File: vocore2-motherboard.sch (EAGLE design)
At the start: 100 parts, among them IC1 AP63205, IC2 FE1.1S, IC3 LM3671MF-3.3, IC4 LM3671MF-3.3, IC5 LM3671MF-3.3, IC7 SN74LVC2G14DBVR, IC8 FT230XS-R, J1 RJHSE-5381, J2 TE_1775470-8, J3 AMPHENOL_1140084168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

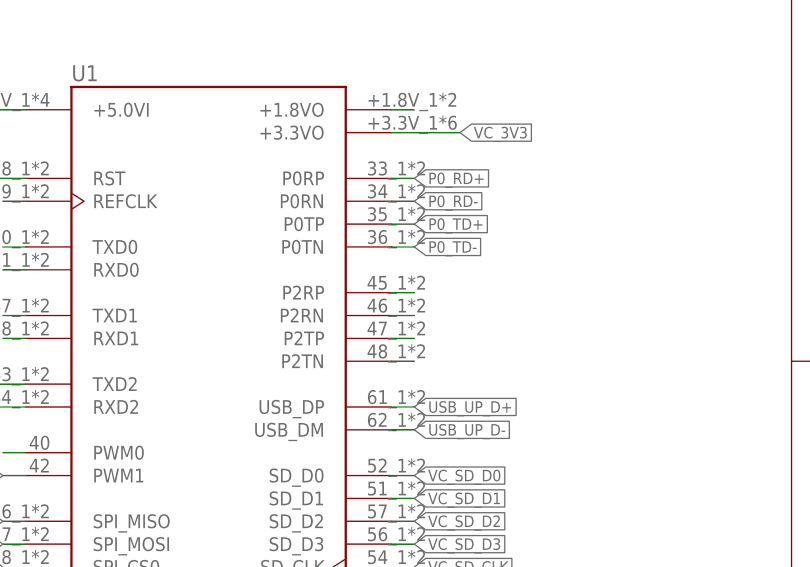
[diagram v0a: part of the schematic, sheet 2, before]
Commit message: fix(pcb): reconnected buzzer
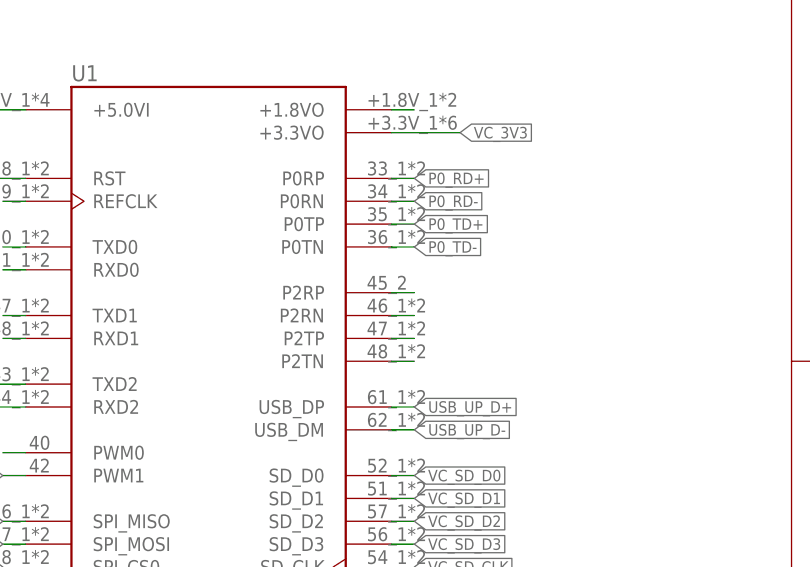
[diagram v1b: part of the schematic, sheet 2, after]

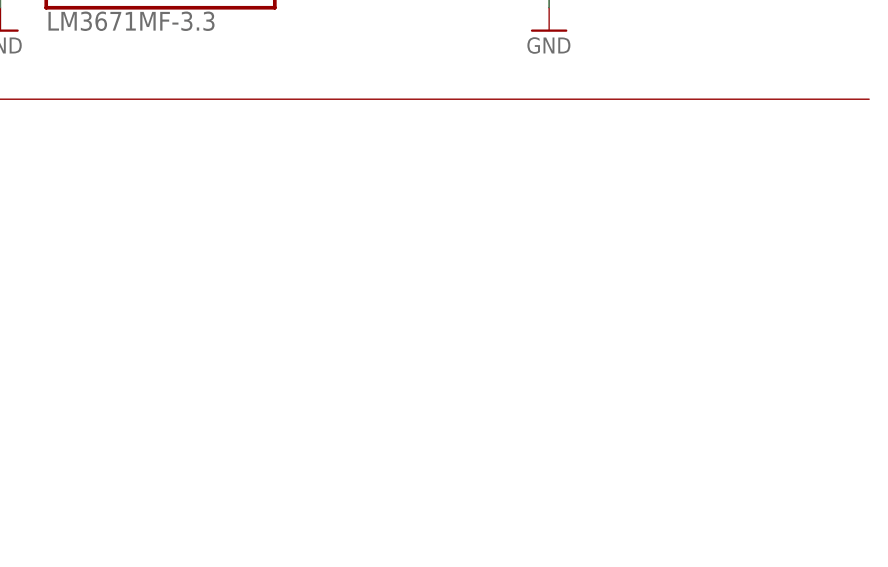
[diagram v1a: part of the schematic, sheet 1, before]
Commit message: feat: 3V3 + GND pinheader for each minipcie-slot
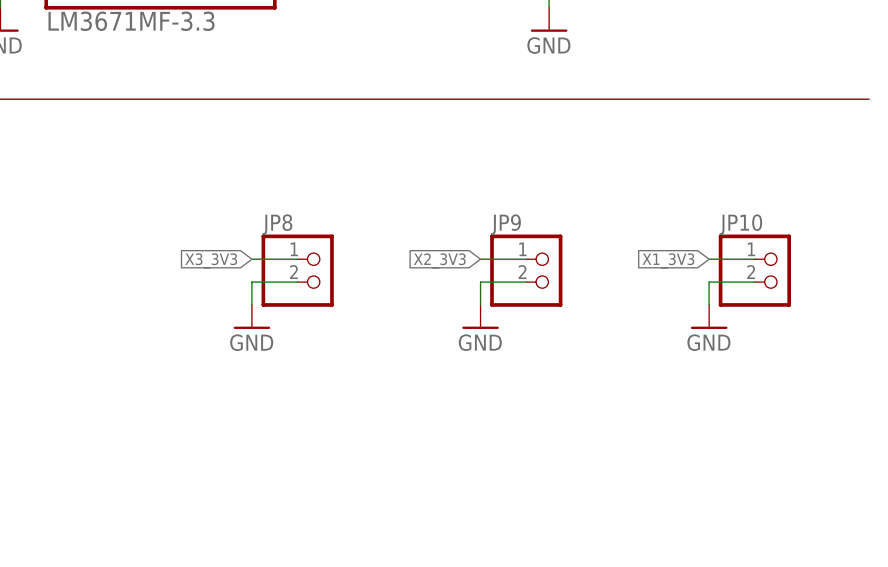
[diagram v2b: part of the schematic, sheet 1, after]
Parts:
- added JP10, JP8, JP9: (no value), pinhead:PINHD-1X2
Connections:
- net GND: now also JP10.2, JP8.2, JP9.2
- net X1_3V3: now also JP10.1
- net X2_3V3: now also JP9.1
- net X3_3V3: now also JP8.1
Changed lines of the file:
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@@
 <part name="GND29" library="supply1" deviceset="GND" device=""/>
 <part name="R22" library="rcl" library_urn="urn:adsk.eagle:library:334" deviceset="R-EU_" device="R0603" package3d_urn="urn:adsk.eagle:package:23555/3" value="330R"/>
+<part name="JP8" library="pinhead" library_urn="urn:adsk.eagle:library:325" deviceset="PINHD-1X2" device="" package3d_urn="urn:adsk.eagle:package:22435/2"/>
+<part name="GND30" library="supply1" deviceset="GND" device=""/>
+<part name="JP9" library="pinhead" library_urn="urn:adsk.eagle:library:325" deviceset="PINHD-1X2" device="" package3d_urn="urn:adsk.eagle:package:22435/2"/>
+<part name="JP10" library="pinhead" library_urn="urn:adsk.eagle:library:325" deviceset="PINHD-1X2" device="" package3d_urn="urn:adsk.eagle:package:22435/2"/>
+<part name="GND45" library="supply1" deviceset="GND" device=""/>
+<part name="GND46" library="supply1" deviceset="GND" device=""/>
 </parts>
 <sheets>
@@
 <attribute name="VALUE" x="132.08" y="33.02" size="1.778" layer="96"/>
 </instance>
+<instance part="JP8" gate="G$1" x="195.58" y="48.26" smashed="yes">
+<attribute name="NAME" x="189.23" y="53.975" size="1.778" layer="95"/>
+<attribute name="VALUE" x="189.23" y="43.18" size="1.778" layer="96"/>
+</instance>
+<instance part="GND30" gate="1" x="187.96" y="43.18" smashed="yes">
+<attribute name="VALUE" x="185.42" y="40.64" size="1.778" layer="96"/>
+</instance>
+<instance part="JP9" gate="G$1" x="220.98" y="48.26" smashed="yes">
+<attribute name="NAME" x="214.63" y="53.975" size="1.778" layer="95"/>
+<attribute name="VALUE" x="214.63" y="43.18" size="1.778" layer="96"/>
+</instance>
+<instance part="JP10" gate="G$1" x="246.38" y="48.26" smashed="yes">
+<attribute name="NAME" x="240.03" y="53.975" size="1.778" layer="95"/>
+<attribute name="VALUE" x="240.03" y="43.18" size="1.778" layer="96"/>
+</instance>
+<instance part="GND45" gate="1" x="213.36" y="43.18" smashed="yes">
+<attribute name="VALUE" x="210.82" y="40.64" size="1.778" layer="96"/>
+</instance>
+<instance part="GND46" gate="1" x="238.76" y="43.18" smashed="yes">
+<attribute name="VALUE" x="236.22" y="40.64" size="1.778" layer="96"/>
+</instance>
 </instances>
 <busses>
@@
 <wire x1="134.62" y1="40.64" x2="134.62" y2="38.1" width="0.1524" layer="91"/>
 <pinref part="GND36" gate="1" pin="GND"/>
+</segment>
+<segment>
+<pinref part="JP8" gate="G$1" pin="2"/>
+<wire x1="193.04" y1="48.26" x2="187.96" y2="48.26" width="0.1524" layer="91"/>
+<wire x1="187.96" y1="48.26" x2="187.96" y2="45.72" width="0.1524" layer="91"/>
+<pinref part="GND30" gate="1" pin="GND"/>
+</segment>
+<segment>
+<pinref part="JP9" gate="G$1" pin="2"/>
+<wire x1="218.44" y1="48.26" x2="213.36" y2="48.26" width="0.1524" layer="91"/>
+<wire x1="213.36" y1="48.26" x2="213.36" y2="45.72" width="0.1524" layer="91"/>
+<pinref part="GND45" gate="1" pin="GND"/>
+</segment>
+<segment>
+<pinref part="JP10" gate="G$1" pin="2"/>
+<wire x1="243.84" y1="48.26" x2="238.76" y2="48.26" width="0.1524" layer="91"/>
+<wire x1="238.76" y1="48.26" x2="238.76" y2="45.72" width="0.1524" layer="91"/>
+<pinref part="GND46" gate="1" pin="GND"/>
 </segment>
 </net>
@@
 <pinref part="R2" gate="G$1" pin="2"/>
 </segment>
+<segment>
+<pinref part="JP10" gate="G$1" pin="1"/>
+<wire x1="243.84" y1="50.8" x2="238.76" y2="50.8" width="0.1524" layer="91"/>
+<label x="238.76" y="50.8" size="1.27" layer="95" rot="R180" xref="yes"/>
+</segment>
 </net>
 <net name="N$6" class="0">
@@
 <pinref part="R4" gate="G$1" pin="2"/>
 </segment>
+<segment>
+<pinref part="JP9" gate="G$1" pin="1"/>
+<wire x1="218.44" y1="50.8" x2="213.36" y2="50.8" width="0.1524" layer="91"/>
+<label x="213.36" y="50.8" size="1.27" layer="95" rot="R180" xref="yes"/>
+</segment>
 </net>
 <net name="X3_3V3" class="0">
@@
 <pinref part="R5" gate="G$1" pin="2"/>
 </segment>
-</net>
+<segment>
+<pinref part="JP8" gate="G$1" pin="1"/>
+<wire x1="193.04" y1="50.8" x2="187.96" y2="50.8" width="0.1524" layer="91"/>
+<label x="187.96" y="50.8" size="1.27" layer="95" rot="R180" xref="yes"/>
+</segment>
+</net>

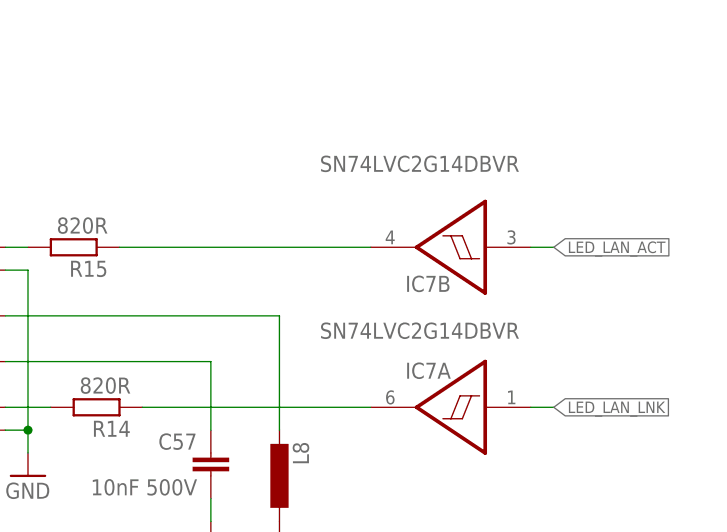
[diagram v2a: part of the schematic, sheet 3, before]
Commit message: fix: use non-inverting buffers to drive lan leds
The rt3050 ethernet switch, integrated on the SoC, has the ability to
configure led polarity. Therefore it is not necessary to fix the
active-low problem in hardware.
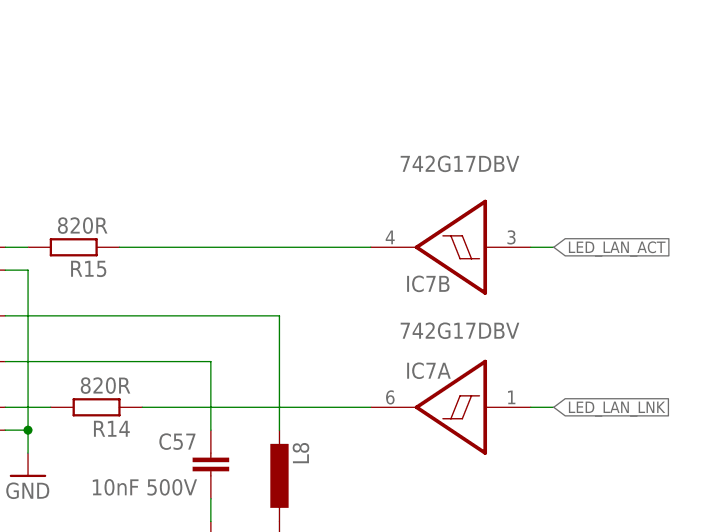
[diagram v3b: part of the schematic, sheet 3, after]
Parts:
- IC7: value SN74LVC2G14DBVR -> 742G17DBV
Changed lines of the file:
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@@
 <attribute name="DIGIKEY" value="A129687CT-ND"/>
 </part>
-<part name="IC7" library="74xx-little-de" library_urn="urn:adsk.eagle:library:86" deviceset="74*2G17" device="DBV" value="SN74LVC2G14DBVR">
+<part name="IC7" library="74xx-little-de" library_urn="urn:adsk.eagle:library:86" deviceset="74*2G17" device="DBV" value="742G17DBV">
 <attribute name="DIGIKEY" value="296-13010-1-ND"/>
 </part>

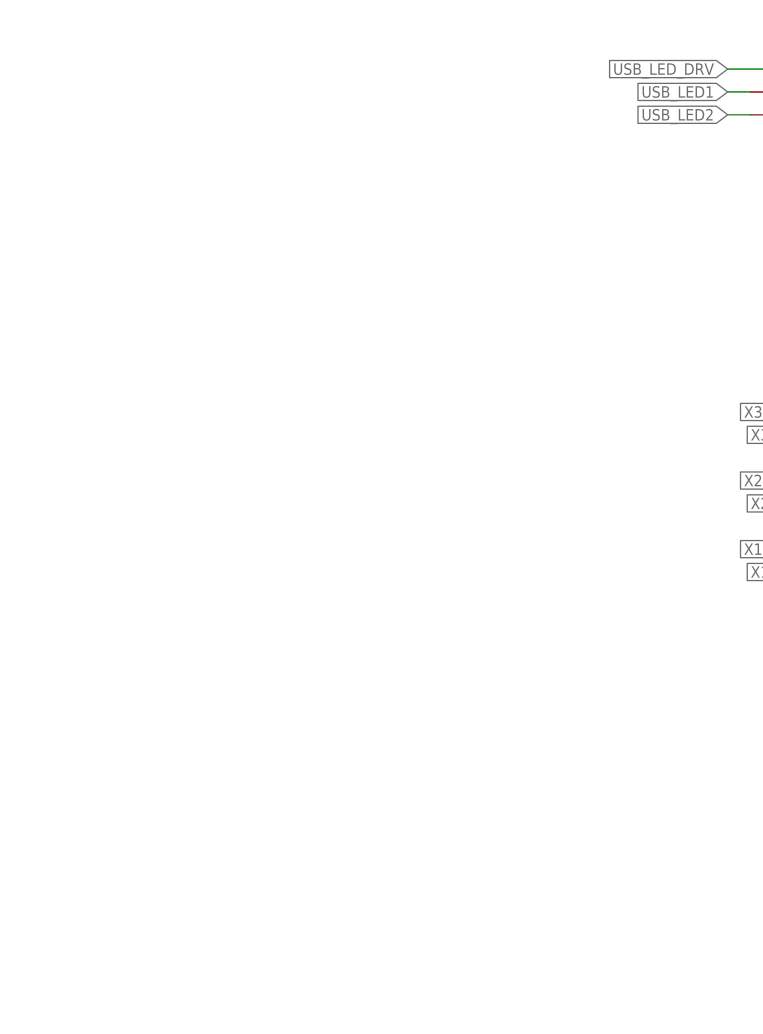
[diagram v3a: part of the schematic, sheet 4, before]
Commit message: feat: TVS diodes on MiniPCIe slots
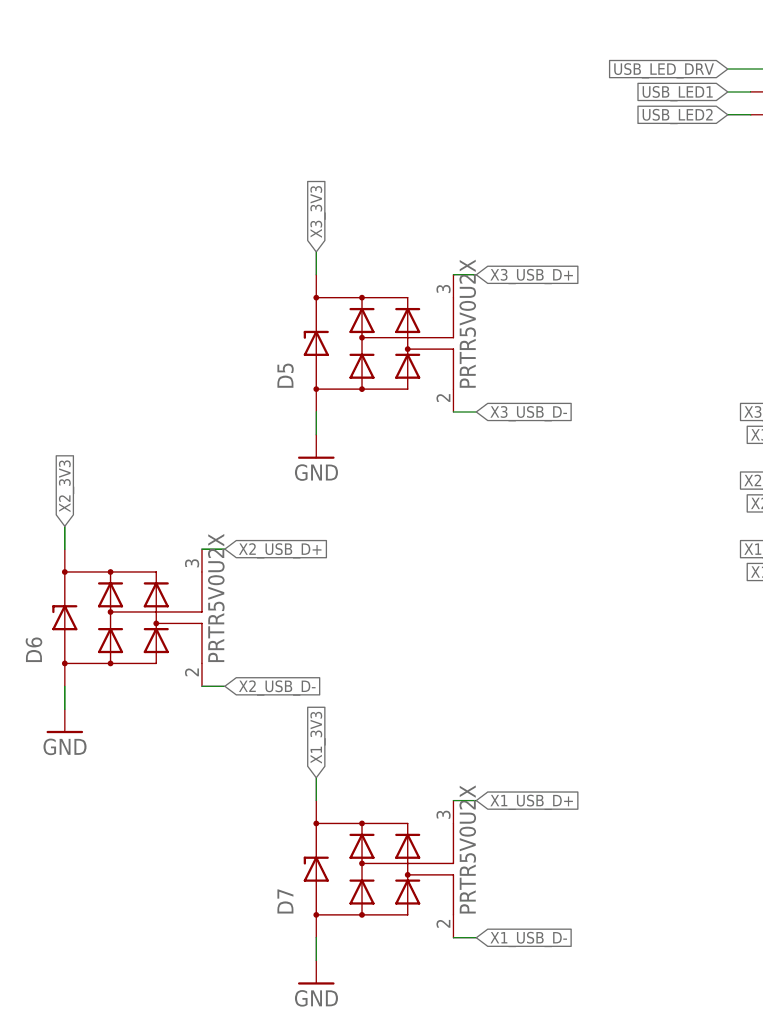
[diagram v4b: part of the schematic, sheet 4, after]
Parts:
- added D5, D6, D7: PRTR5V0U2X, diode:PRTR5V0U2X
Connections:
- net GND: now also D5.GND, D6.GND, D7.GND
- net X1_3V3: now also D7.VCC
- net X1_USB_D+: now also D7.IO2
- net X1_USB_D-: now also D7.IO1
- net X2_3V3: now also D6.VCC
- net X2_USB_D+: now also D6.IO2
- net X2_USB_D-: now also D6.IO1
- net X3_3V3: now also D5.VCC
- net X3_USB_D+: now also D5.IO2
- net X3_USB_D-: now also D5.IO1
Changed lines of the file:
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@@
 <part name="GND45" library="supply1" deviceset="GND" device=""/>
 <part name="GND46" library="supply1" deviceset="GND" device=""/>
+<part name="D5" library="diode" library_urn="urn:adsk.eagle:library:210" deviceset="PRTR5V0U2X" device="">
+<attribute name="DIGIKEY" value="1727-3884-1-ND"/>
+<attribute name="FARNELL" value="1524157"/>
+</part>
+<part name="D6" library="diode" library_urn="urn:adsk.eagle:library:210" deviceset="PRTR5V0U2X" device="">
+<attribute name="DIGIKEY" value="1727-3884-1-ND"/>
+<attribute name="FARNELL" value="1524157"/>
+</part>
+<part name="D7" library="diode" library_urn="urn:adsk.eagle:library:210" deviceset="PRTR5V0U2X" device="">
+<attribute name="DIGIKEY" value="1727-3884-1-ND"/>
+<attribute name="FARNELL" value="1524157"/>
+</part>
+<part name="GND47" library="supply1" library_urn="urn:adsk.eagle:library:371" deviceset="GND" device="">
+<attribute name="SPICEPREFIX" value="G"/>
+</part>
+<part name="GND48" library="supply1" library_urn="urn:adsk.eagle:library:371" deviceset="GND" device="">
+<attribute name="SPICEPREFIX" value="G"/>
+</part>
+<part name="GND49" library="supply1" library_urn="urn:adsk.eagle:library:371" deviceset="GND" device="">
+<attribute name="SPICEPREFIX" value="G"/>
+</part>
 </parts>
 <sheets>
@@
 <attribute name="VALUE" x="153.035" y="53.848" size="1.778" layer="96" rot="R90"/>
 <attribute name="DIGIKEY" x="147.32" y="58.42" size="1.778" layer="96" display="off"/>
+</instance>
+<instance part="D5" gate="G$1" x="-22.86" y="38.1" smashed="yes" rot="R90">
+<attribute name="FARNELL" x="-22.86" y="38.1" size="1.778" layer="96" rot="R90" display="off"/>
+<attribute name="NAME" x="-33.02" y="32.9565" size="1.778" layer="95" rot="R90"/>
+<attribute name="VALUE" x="-12.7635" y="32.9565" size="1.778" layer="96" rot="R90"/>
+<attribute name="DIGIKEY" x="-22.86" y="38.1" size="1.778" layer="96" rot="R90" display="off"/>
+</instance>
+<instance part="D6" gate="G$1" x="-50.8" y="7.62" smashed="yes" rot="R90">
+<attribute name="FARNELL" x="-50.8" y="7.62" size="1.778" layer="96" rot="R90" display="off"/>
+<attribute name="NAME" x="-60.96" y="2.4765" size="1.778" layer="95" rot="R90"/>
+<attribute name="VALUE" x="-40.7035" y="2.4765" size="1.778" layer="96" rot="R90"/>
+<attribute name="DIGIKEY" x="-50.8" y="7.62" size="1.778" layer="96" rot="R90" display="off"/>
+</instance>
+<instance part="D7" gate="G$1" x="-22.86" y="-20.32" smashed="yes" rot="R90">
+<attribute name="FARNELL" x="-22.86" y="-20.32" size="1.778" layer="96" rot="R90" display="off"/>
+<attribute name="NAME" x="-33.02" y="-25.4635" size="1.778" layer="95" rot="R90"/>
+<attribute name="VALUE" x="-12.7635" y="-25.4635" size="1.778" layer="96" rot="R90"/>
+<attribute name="DIGIKEY" x="-22.86" y="-20.32" size="1.778" layer="96" rot="R90" display="off"/>
+</instance>
+<instance part="GND47" gate="1" x="-30.48" y="25.4" smashed="yes" rot="MR0">
+<attribute name="VALUE" x="-27.94" y="22.86" size="1.778" layer="96" rot="MR0"/>
+</instance>
+<instance part="GND48" gate="1" x="-58.42" y="-5.08" smashed="yes" rot="MR0">
+<attribute name="VALUE" x="-55.88" y="-7.62" size="1.778" layer="96" rot="MR0"/>
+</instance>
+<instance part="GND49" gate="1" x="-30.48" y="-33.02" smashed="yes" rot="MR0">
+<attribute name="VALUE" x="-27.94" y="-35.56" size="1.778" layer="96" rot="MR0"/>
 </instance>
 </instances>
@@
 <pinref part="GND23" gate="1" pin="GND"/>
 </segment>
+<segment>
+<pinref part="D5" gate="G$1" pin="GND"/>
+<wire x1="-30.48" y1="30.48" x2="-30.48" y2="27.94" width="0.1524" layer="91"/>
+<pinref part="GND47" gate="1" pin="GND"/>
+</segment>
+<segment>
+<pinref part="D6" gate="G$1" pin="GND"/>
+<wire x1="-58.42" y1="0" x2="-58.42" y2="-2.54" width="0.1524" layer="91"/>
+<pinref part="GND48" gate="1" pin="GND"/>
+</segment>
+<segment>
+<pinref part="D7" gate="G$1" pin="GND"/>
+<wire x1="-30.48" y1="-27.94" x2="-30.48" y2="-30.48" width="0.1524" layer="91"/>
+<pinref part="GND49" gate="1" pin="GND"/>
+</segment>
 </net>
 <net name="USB_UP_D-" class="0">
@@
 <label x="27.94" y="15.24" size="1.27" layer="95" rot="MR0" xref="yes"/>
 </segment>
+<segment>
+<pinref part="D7" gate="G$1" pin="IO2"/>
+<wire x1="-15.24" y1="-12.7" x2="-12.7" y2="-12.7" width="0.1524" layer="91"/>
+<label x="-12.7" y="-12.7" size="1.27" layer="95" xref="yes"/>
+</segment>
 </net>
 <net name="X1_USB_D-" class="0">
@@
 <label x="27.94" y="12.7" size="1.27" layer="95" rot="MR0" xref="yes"/>
 </segment>
+<segment>
+<pinref part="D7" gate="G$1" pin="IO1"/>
+<wire x1="-15.24" y1="-27.94" x2="-12.7" y2="-27.94" width="0.1524" layer="91"/>
+<label x="-12.7" y="-27.94" size="1.27" layer="95" xref="yes"/>
+</segment>
 </net>
 <net name="X3_USB_D+" class="0">
@@
 <wire x1="30.48" y1="30.48" x2="27.94" y2="30.48" width="0.1524" layer="91"/>
 </segment>
+<segment>
+<pinref part="D5" gate="G$1" pin="IO2"/>
+<wire x1="-15.24" y1="45.72" x2="-12.7" y2="45.72" width="0.1524" layer="91"/>
+<label x="-12.7" y="45.72" size="1.27" layer="95" xref="yes"/>
+</segment>
 </net>
 <net name="X3_USB_D-" class="0">
@@
 <pinref part="IC2" gate="G$1" pin="DM2"/>
 <wire x1="27.94" y1="27.94" x2="30.48" y2="27.94" width="0.1524" layer="91"/>
+</segment>
+<segment>
+<pinref part="D5" gate="G$1" pin="IO1"/>
+<wire x1="-15.24" y1="30.48" x2="-12.7" y2="30.48" width="0.1524" layer="91"/>
+<label x="-12.7" y="30.48" size="1.27" layer="95" xref="yes"/>
 </segment>
 </net>
@@
 <label x="157.48" y="111.76" size="1.27" layer="95" xref="yes"/>
 </segment>
+<segment>
+<pinref part="D6" gate="G$1" pin="IO2"/>
+<wire x1="-43.18" y1="15.24" x2="-40.64" y2="15.24" width="0.1524" layer="91"/>
+<label x="-40.64" y="15.24" size="1.27" layer="95" xref="yes"/>
+</segment>
 </net>
 <net name="X2_USB_D-" class="0">
@@
 <wire x1="149.86" y1="114.3" x2="157.48" y2="114.3" width="0.1524" layer="91"/>
 <label x="157.48" y="114.3" size="1.27" layer="95" xref="yes"/>
+</segment>
+<segment>
+<pinref part="D6" gate="G$1" pin="IO1"/>
+<wire x1="-43.18" y1="0" x2="-40.64" y2="0" width="0.1524" layer="91"/>
+<label x="-40.64" y="0" size="1.27" layer="95" xref="yes"/>
 </segment>
 </net>
@@
 <label x="22.86" y="109.22" size="1.27" layer="95" rot="R180" xref="yes"/>
 </segment>
+<segment>
+<pinref part="D5" gate="G$1" pin="VCC"/>
+<wire x1="-30.48" y1="45.72" x2="-30.48" y2="48.26" width="0.1524" layer="91"/>
+<label x="-30.48" y="48.26" size="1.27" layer="95" rot="R90" xref="yes"/>
+</segment>
 </net>
 <net name="X2_3V3" class="0">
@@
 <label x="111.76" y="109.22" size="1.27" layer="95" rot="R180" xref="yes"/>
 </segment>
+<segment>
+<pinref part="D6" gate="G$1" pin="VCC"/>
+<wire x1="-58.42" y1="15.24" x2="-58.42" y2="17.78" width="0.1524" layer="91"/>
+<label x="-58.42" y="17.78" size="1.27" layer="95" rot="R90" xref="yes"/>
+</segment>
 </net>
 <net name="X1_3V3" class="0">
@@
 <label x="195.58" y="109.22" size="1.27" layer="95" rot="R180" xref="yes"/>
 </segment>
-</net>
+<segment>
+<pinref part="D7" gate="G$1" pin="VCC"/>
+<wire x1="-30.48" y1="-12.7" x2="-30.48" y2="-10.16" width="0.1524" layer="91"/>
+<label x="-30.48" y="-10.16" size="1.27" layer="95" rot="R90" xref="yes"/>
+</segment>
+</net>
